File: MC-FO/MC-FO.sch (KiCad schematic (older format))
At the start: 0 parts

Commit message: Add files via upload
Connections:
- wire segments 7 -> 10
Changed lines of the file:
@@
 $Descr A4 11693 8268
 encoding utf-8
-Sheet 1 6
+Sheet 1 12
 Title ""
 Date ""
@@
 Comment4 ""
 $EndDescr
+Text GLabel 7900 1150 0    50   Input ~ 0
+3V3
+Text GLabel 7900 1350 0    50   Input ~ 0
+5V
+$Comp
+L power:GND #PWR?
+U 1 1 6175A5B5
+P 7850 1550
+F 0 "#PWR?" H 7850 1300 50  0001 C CNN
+F 1 "GND" H 7855 1377 50  0000 C CNN
+F 2 "" H 7850 1550 50  0001 C CNN
+F 3 "" H 7850 1550 50  0001 C CNN
+	1    7850 1550
+	1    0    0    -1
+$EndComp
+Wire Wire Line
+	3500 1350 4200 1350
+Wire Wire Line
+	3500 3850 4350 3850
 $Sheet
-S 3150 3100 750  250
+S 2750 6700 750  250
+U 6175C442
+F0 "Sheet6175C441" 50
+F1 "Voltage_Regulation.sch" 50
+F2 "Vdd" I R 3500 6850 50
+$EndSheet
+$Sheet
+S 2750 3100 750  300
+U 61750A2A
+F0 "Emitter3" 50
+F1 "Emitter_Circuits.sch" 50
+F2 "EPWM" I R 3500 3300 50
+$EndSheet
+$Sheet
+S 2750 2600 750  250
+U 617509F7
+F0 "Emmiter2" 50
+F1 "Emitter_Circuits.sch" 50
+F2 "EPWM" I R 3500 2750 50
+$EndSheet
+$Sheet
+S 2750 2050 750  250
 U 61717EAF
 F0 "Emitter1" 50
 F1 "Emitter_Circuits.sch" 50
-F2 "EPWM" I R 3900 3200 50
+F2 "EPWM" I R 3500 2150 50
 $EndSheet
 $Sheet
-S 3150 3600 800  300
-U 617509F7
-F0 "Emmiter2" 50
-F1 "Emitter_Circuits.sch" 50
-F2 "EPWM" I R 3950 3750 50
+S 2750 3700 750  250
+U 6171C819
+F0 "Detector1" 50
+F1 "Detector_Circuits.sch" 50
+F2 "EPWM" I R 3500 3850 50
 $EndSheet
 $Sheet
-S 3150 4200 800  300
-U 61750A2A
-F0 "Emitter3" 50
+S 2750 1200 750  250
+U 6175812E
+F0 "Status LED" 50
+F1 "MC-LED.sch" 50
+F2 "StatusLED" I R 3500 1350 50
+$EndSheet
+Wire Wire Line
+	3500 2150 4100 2150
+$Sheet
+S 2750 6050 750  250
+U 61724A08
+F0 "Detector2" 50
+F1 "Detector_Circuits.sch" 50
+F2 "EPWM" I R 3500 6200 50
+$EndSheet
+Wire Wire Line
+	3500 2750 4200 2750
+Wire Wire Line
+	3500 3300 4200 3300
+Wire Wire Line
+	3500 6850 4200 6850
+Wire Wire Line
+	3500 6200 4350 6200
+$Sheet
+S 2750 700  750  250
+U 61766F1E
+F0 "Power LED" 50
+F1 "MC-Power_LED.sch" 50
+F2 "Vdd" I R 3500 850 50
+$EndSheet
+Wire Wire Line
+	3500 850  4200 850
+Wire Wire Line
+	4200 850  4200 800
+Wire Wire Line
+	4200 800  4250 800
+$Sheet
+S 2750 4350 750  250
+U 6176CA10
+F0 "Emitter4" 50
 F1 "Emitter_Circuits.sch" 50
-F2 "EPWM" I R 3950 4400 50
 $EndSheet
-Text GLabel 5350 2650 0    50   Input ~ 0
-3V3
-Text GLabel 5350 2850 0    50   Input ~ 0
-5V
 $Sheet
-S 3350 2150 600  300
-U 6175812E
-F0 "Sheet6175812D" 50
-F1 "MC-LED.sch" 50
-F2 "StatusLED" I R 3950 2300 50
+S 2750 4900 750  250
+U 6176CA81
+F0 "Emitter5" 50
+F1 "Emitter_Circuits.sch" 50
 $EndSheet
-$Comp
-L power:GND #PWR?
-U 1 1 6175A5B5
-P 5250 3000
-F 0 "#PWR?" H 5250 2750 50  0001 C CNN
-F 1 "GND" H 5255 2827 50  0000 C CNN
-F 2 "" H 5250 3000 50  0001 C CNN
-F 3 "" H 5250 3000 50  0001 C CNN
-	1    5250 3000
-	1    0    0    -1
-$EndComp
-Wire Wire Line
-	3950 2300 4650 2300
-Wire Wire Line
-	4650 2300 4650 3350
-Wire Wire Line
-	4650 3350 5350 3350
-Wire Wire Line
-	5350 3350 5350 3300
-Wire Wire Line
-	3900 3200 4450 3200
-Wire Wire Line
-	4450 3200 4450 3550
-Wire Wire Line
-	4450 3550 5300 3550
 $Sheet
-S 3150 4800 900  250
-U 6175C442
-F0 "Sheet6175C441" 50
-F1 "Voltage_Regulation.sch" 50
-F2 "Vdd" I R 4050 4950 50
+S 2750 5450 750  250
+U 6176CAE4
+F0 "Emitter6" 50
+F1 "Emitter_Circuits.sch" 50
 $EndSheet
 $EndSCHEMATC

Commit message: Add files via upload
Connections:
- wire segments 10 -> 13
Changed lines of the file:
@@
 S 2750 6700 750  250
 U 6175C442
-F0 "Sheet6175C441" 50
+F0 "Voltage Regulation" 50
 F1 "Voltage_Regulation.sch" 50
 F2 "Vdd" I R 3500 6850 50
@@
 F0 "Detector1" 50
 F1 "Detector_Circuits.sch" 50
-F2 "EPWM" I R 3500 3850 50
+F2 "DPWM" I R 3500 3850 50
 $EndSheet
 $Sheet
@@
 F0 "Detector2" 50
 F1 "Detector_Circuits.sch" 50
-F2 "EPWM" I R 3500 6200 50
+F2 "DPWM" I R 3500 6200 50
 $EndSheet
 Wire Wire Line
@@
 F0 "Emitter4" 50
 F1 "Emitter_Circuits.sch" 50
+F2 "EPWM" I R 3500 4500 50
 $EndSheet
 $Sheet
@@
 F0 "Emitter5" 50
 F1 "Emitter_Circuits.sch" 50
+F2 "EPWM" I R 3500 5050 50
 $EndSheet
 $Sheet
@@
 F0 "Emitter6" 50
 F1 "Emitter_Circuits.sch" 50
+F2 "EPWM" I R 3500 5600 50
 $EndSheet
+Wire Wire Line
+	3500 5600 4350 5600
+Wire Wire Line
+	3500 5050 4400 5050
+Wire Wire Line
+	3500 4500 4450 4500
 $EndSCHEMATC

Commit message: Add files via upload
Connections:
- net labels added: 24V, GND1, GND2, GPIO
- wire segments 13 -> 55
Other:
- note added: "is the vreg sheet supposed to supply the 3v3 and 5 v \nvoltages to the detectors and emitters?"
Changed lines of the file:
@@
 $Descr A4 11693 8268
 encoding utf-8
-Sheet 1 12
+Sheet 1 11
 Title ""
 Date ""
@@
 Comment4 ""
 $EndDescr
-Text GLabel 7900 1150 0    50   Input ~ 0
+Text GLabel 10450 5150 0    50   Input ~ 0
 3V3
-Text GLabel 7900 1350 0    50   Input ~ 0
+Text GLabel 10450 5350 0    50   Input ~ 0
 5V
 $Comp
 L power:GND #PWR?
 U 1 1 6175A5B5
-P 7850 1550
-F 0 "#PWR?" H 7850 1300 50  0001 C CNN
-F 1 "GND" H 7855 1377 50  0000 C CNN
-F 2 "" H 7850 1550 50  0001 C CNN
-F 3 "" H 7850 1550 50  0001 C CNN
-	1    7850 1550
+P 10400 5550
+F 0 "#PWR?" H 10400 5300 50  0001 C CNN
+F 1 "GND" H 10405 5377 50  0000 C CNN
+F 2 "" H 10400 5550 50  0001 C CNN
+F 3 "" H 10400 5550 50  0001 C CNN
+	1    10400 5550
 	1    0    0    -1
 $EndComp
 Wire Wire Line
-	3500 1350 4200 1350
-Wire Wire Line
-	3500 3850 4350 3850
-$Sheet
-S 2750 6700 750  250
+	7250 2200 6550 2200
+$Sheet
+S 1500 4500 1000 500
+U 6176CA10
+F0 "Emitter4" 50
+F1 "Emitter_Circuits.sch" 50
+F2 "EPWM" I R 2500 4650 50
+F3 "5V" I R 2500 4800 50
+F4 "GND2" I R 2500 4900 50
+$EndSheet
+$Sheet
+S 1500 5500 1000 500
+U 6176CA81
+F0 "Emitter5" 50
+F1 "Emitter_Circuits.sch" 50
+F2 "EPWM" I R 2500 5600 50
+F3 "5V" I R 2500 5750 50
+F4 "GND2" I R 2500 5900 50
+$EndSheet
+$Sheet
+S 1500 6500 1000 500
+U 6176CAE4
+F0 "Emitter6" 50
+F1 "Emitter_Circuits.sch" 50
+F2 "EPWM" I R 2500 6600 50
+F3 "5V" I R 2500 6750 50
+F4 "GND2" I R 2500 6900 50
+$EndSheet
+$Sheet
+S 1500 1500 1000 500
+U 61717EAF
+F0 "Emitter1" 50
+F1 "Emitter_Circuits.sch" 50
+F2 "EPWM" I R 2500 1600 50
+F3 "5V" I R 2500 1750 50
+F4 "GND2" I R 2500 1900 50
+$EndSheet
+$Sheet
+S 1500 2500 1000 500
+U 617509F7
+F0 "Emmiter2" 50
+F1 "Emitter_Circuits.sch" 50
+F2 "EPWM" I R 2500 2600 50
+F3 "5V" I R 2500 2750 50
+F4 "GND2" I R 2500 2900 50
+$EndSheet
+$Sheet
+S 1500 3500 1000 500
+U 61750A2A
+F0 "Emitter3" 50
+F1 "Emitter_Circuits.sch" 50
+F2 "EPWM" I R 2500 3700 50
+F3 "5V" I R 2500 3850 50
+F4 "GND2" I R 2500 3950 50
+$EndSheet
+Text HLabel 9300 800  2    79   Input ~ 0
+24V
+Wire Wire Line
+	2500 2600 3200 2600
+Wire Wire Line
+	2500 3700 3200 3700
+Wire Wire Line
+	2500 4650 3250 4650
+Wire Wire Line
+	2500 5600 3400 5600
+Wire Wire Line
+	2500 1600 3100 1600
+Wire Wire Line
+	3500 1750 2500 1750
+Wire Wire Line
+	3500 6750 2500 6750
+Wire Wire Line
+	2500 5750 3500 5750
+Connection ~ 3500 5750
+Wire Wire Line
+	2500 4800 3500 4800
+Connection ~ 3500 4800
+Wire Wire Line
+	2500 3850 3500 3850
+Connection ~ 3500 3850
+Wire Wire Line
+	3500 3850 3500 4750
+Wire Wire Line
+	2500 2750 3500 2750
+Connection ~ 3500 2750
+Wire Wire Line
+	3500 4800 3500 4750
+Connection ~ 3500 4750
+Wire Wire Line
+	3500 5750 3500 6750
+Wire Wire Line
+	4950 5750 3500 5750
+Wire Wire Line
+	4950 4750 3500 4750
+Wire Wire Line
+	4950 5600 4100 5600
+$Sheet
+S 4950 5500 1000 500
+U 61724A08
+F0 "Detector2" 50
+F1 "Detector_Circuits.sch" 50
+F2 "DPWM" I L 4950 5600 50
+F3 "5V" I L 4950 5750 50
+F4 "GND2" I L 4950 5900 50
+$EndSheet
+$Sheet
+S 4950 4500 1000 500
+U 6171C819
+F0 "Detector1" 50
+F1 "Detector_Circuits.sch" 50
+F2 "DPWM" I L 4950 4600 50
+F3 "5V" I L 4950 4750 50
+F4 "GND2" I L 4950 4900 50
+$EndSheet
+Wire Wire Line
+	4950 4600 4100 4600
+$Sheet
+S 7250 1150 1000 500
 U 6175C442
 F0 "Voltage Regulation" 50
 F1 "Voltage_Regulation.sch" 50
-F2 "Vdd" I R 3500 6850 50
-$EndSheet
-$Sheet
-S 2750 3100 750  300
-U 61750A2A
-F0 "Emitter3" 50
-F1 "Emitter_Circuits.sch" 50
-F2 "EPWM" I R 3500 3300 50
-$EndSheet
-$Sheet
-S 2750 2600 750  250
-U 617509F7
-F0 "Emmiter2" 50
-F1 "Emitter_Circuits.sch" 50
-F2 "EPWM" I R 3500 2750 50
-$EndSheet
-$Sheet
-S 2750 2050 750  250
-U 61717EAF
-F0 "Emitter1" 50
-F1 "Emitter_Circuits.sch" 50
-F2 "EPWM" I R 3500 2150 50
-$EndSheet
-$Sheet
-S 2750 3700 750  250
-U 6171C819
-F0 "Detector1" 50
-F1 "Detector_Circuits.sch" 50
-F2 "DPWM" I R 3500 3850 50
-$EndSheet
-$Sheet
-S 2750 1200 750  250
+F2 "Vdd" I R 8250 1300 50
+F3 "3V3" I L 7250 1550 50
+F4 "5V" I L 7250 1250 50
+F5 "GND1" I L 7250 1400 50
+$EndSheet
+Text Notes 6250 1000 0    50   ~ 0
+is the vreg sheet supposed to supply the 3v3 and 5 v \nvoltages to the detectors and emitters?
+Wire Wire Line
+	3500 2750 3500 3850
+$Sheet
+S 7250 2100 1000 500
 U 6175812E
 F0 "Status LED" 50
 F1 "MC-LED.sch" 50
-F2 "StatusLED" I R 3500 1350 50
-$EndSheet
-Wire Wire Line
-	3500 2150 4100 2150
-$Sheet
-S 2750 6050 750  250
-U 61724A08
-F0 "Detector2" 50
-F1 "Detector_Circuits.sch" 50
-F2 "DPWM" I R 3500 6200 50
-$EndSheet
-Wire Wire Line
-	3500 2750 4200 2750
-Wire Wire Line
-	3500 3300 4200 3300
-Wire Wire Line
-	3500 6850 4200 6850
-Wire Wire Line
-	3500 6200 4350 6200
-$Sheet
-S 2750 700  750  250
-U 61766F1E
-F0 "Power LED" 50
-F1 "MC-Power_LED.sch" 50
-F2 "Vdd" I R 3500 850 50
-$EndSheet
-Wire Wire Line
-	3500 850  4200 850
-Wire Wire Line
-	4200 850  4200 800
-Wire Wire Line
-	4200 800  4250 800
-$Sheet
-S 2750 4350 750  250
-U 6176CA10
-F0 "Emitter4" 50
-F1 "Emitter_Circuits.sch" 50
-F2 "EPWM" I R 3500 4500 50
-$EndSheet
-$Sheet
-S 2750 4900 750  250
-U 6176CA81
-F0 "Emitter5" 50
-F1 "Emitter_Circuits.sch" 50
-F2 "EPWM" I R 3500 5050 50
-$EndSheet
-$Sheet
-S 2750 5450 750  250
-U 6176CAE4
-F0 "Emitter6" 50
-F1 "Emitter_Circuits.sch" 50
-F2 "EPWM" I R 3500 5600 50
-$EndSheet
-Wire Wire Line
-	3500 5600 4350 5600
-Wire Wire Line
-	3500 5050 4400 5050
-Wire Wire Line
-	3500 4500 4450 4500
+F2 "StatusLED" I L 7250 2200 50
+F3 "3V3" I L 7250 2350 50
+F4 "GND1" I L 7250 2500 50
+$EndSheet
+Wire Wire Line
+	9300 800  8750 800
+Wire Wire Line
+	8750 800  8750 1300
+Wire Wire Line
+	8250 1300 8750 1300
+Connection ~ 3500 1750
+Wire Wire Line
+	3500 1750 3500 2750
+Wire Wire Line
+	7250 1250 3500 1250
+Wire Wire Line
+	3500 1250 3500 1750
+Wire Wire Line
+	7250 1550 5550 1550
+Wire Wire Line
+	5550 1550 5550 2350
+Wire Wire Line
+	5550 2350 7250 2350
+Wire Wire Line
+	2500 1900 2850 1900
+Wire Wire Line
+	2850 1900 2850 2900
+Wire Wire Line
+	2500 6900 2850 6900
+Wire Wire Line
+	2850 6900 2850 6950
+Connection ~ 2850 6900
+Wire Wire Line
+	2500 5900 2850 5900
+Connection ~ 2850 5900
+Wire Wire Line
+	2850 5900 2850 6900
+Wire Wire Line
+	2500 3950 2850 3950
+Connection ~ 2850 3950
+Wire Wire Line
+	2850 3950 2850 4900
+Wire Wire Line
+	2500 4900 2850 4900
+Connection ~ 2850 4900
+Wire Wire Line
+	2850 4900 2850 5900
+Wire Wire Line
+	2500 2900 2850 2900
+Connection ~ 2850 2900
+Wire Wire Line
+	2850 2900 2850 3950
+Wire Wire Line
+	3200 6600 3200 6550
+Wire Wire Line
+	2500 6600 3200 6600
+Wire Wire Line
+	3500 4800 3500 5750
+Wire Wire Line
+	4950 4900 4300 4900
+Wire Wire Line
+	4300 4900 4300 5900
+Wire Wire Line
+	4950 5900 4300 5900
+Connection ~ 4300 5900
+Wire Wire Line
+	4300 5900 4300 6950
+$Comp
+L power:GND1 #PWR?
+U 1 1 617C7B3D
+P 6850 2950
+F 0 "#PWR?" H 6850 2700 50  0001 C CNN
+F 1 "GND1" H 6855 2777 50  0000 C CNN
+F 2 "" H 6850 2950 50  0001 C CNN
+F 3 "" H 6850 2950 50  0001 C CNN
+	1    6850 2950
+	1    0    0    -1
+$EndComp
+Wire Wire Line
+	7250 1400 6850 1400
+Wire Wire Line
+	6850 1400 6850 2500
+Wire Wire Line
+	7250 2500 6850 2500
+Connection ~ 6850 2500
+$Comp
+L power:GND2 #PWR?
+U 1 1 617BB8F9
+P 3750 7350
+F 0 "#PWR?" H 3750 7100 50  0001 C CNN
+F 1 "GND2" H 3755 7177 50  0000 C CNN
+F 2 "" H 3750 7350 50  0001 C CNN
+F 3 "" H 3750 7350 50  0001 C CNN
+	1    3750 7350
+	1    0    0    -1
+$EndComp
+Wire Wire Line
+	3750 6950 3750 7350
+Wire Wire Line
+	2850 6950 3750 6950
+Wire Wire Line
+	4300 6950 3750 6950
+Connection ~ 3750 6950
+Text HLabel 6550 2200 0    50   Input ~ 0
+GPIO
+Wire Wire Line
+	6850 2500 6850 2950
 $EndSCHEMATC

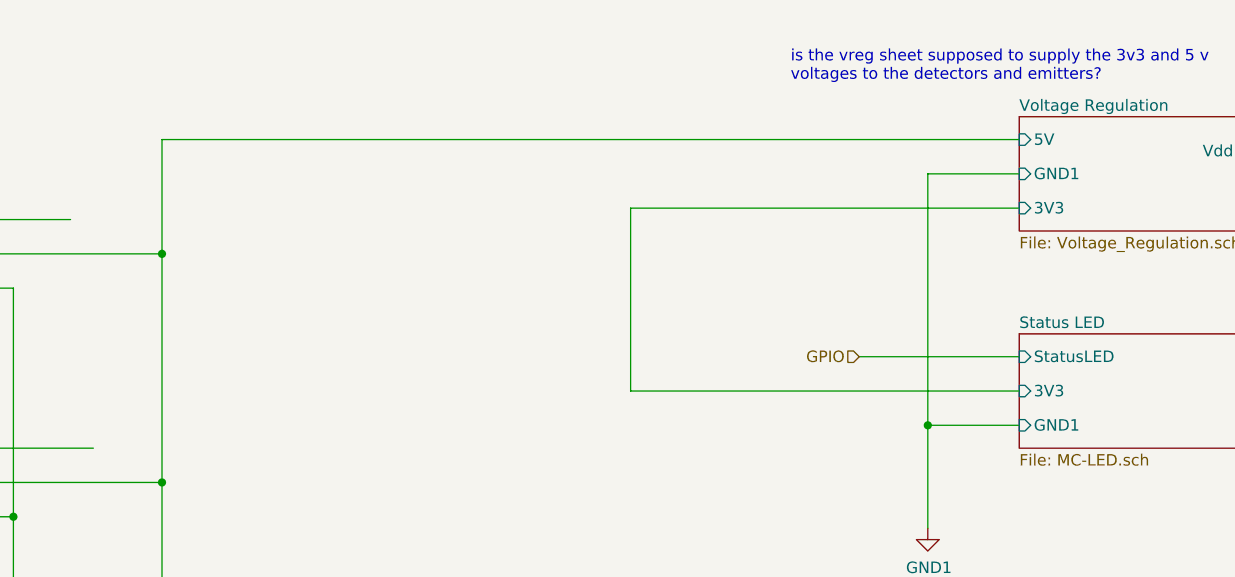
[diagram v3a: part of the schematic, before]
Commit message: Updated LED Ckts, Added new IC model
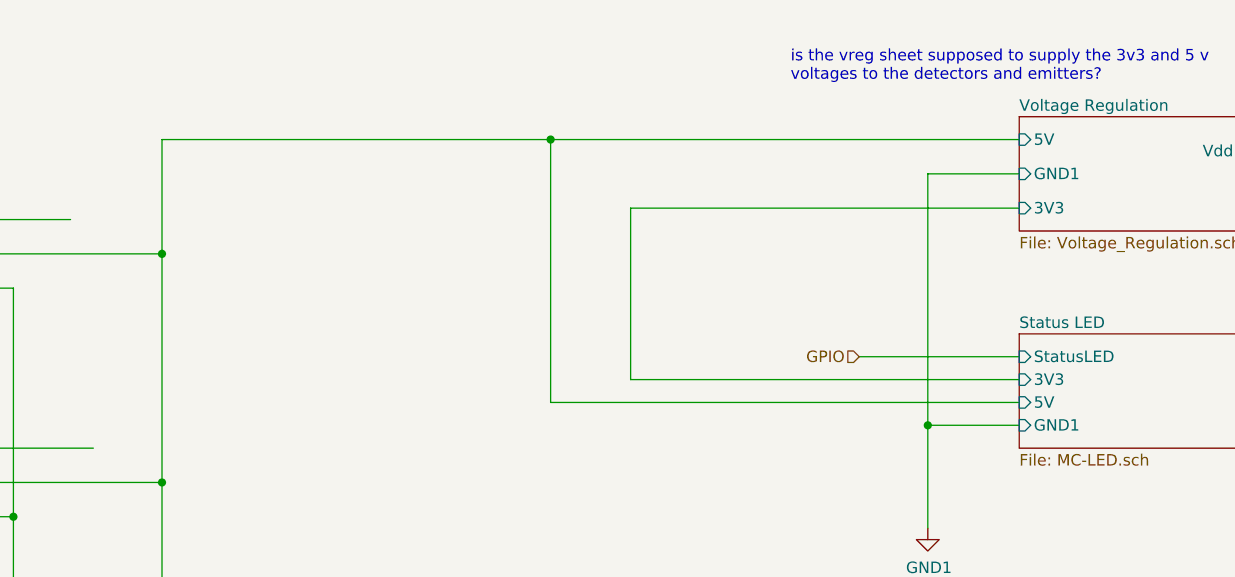
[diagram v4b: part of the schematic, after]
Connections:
- wire segments 55 -> 58
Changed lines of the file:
@@
 F1 "MC-LED.sch" 50
 F2 "StatusLED" I L 7250 2200 50
-F3 "3V3" I L 7250 2350 50
+F3 "3V3" I L 7250 2300 50
 F4 "GND1" I L 7250 2500 50
+F5 "5V" I L 7250 2400 50
 $EndSheet
 Wire Wire Line
@@
 	3500 1750 3500 2750
 Wire Wire Line
-	7250 1250 3500 1250
+	7250 1250 5200 1250
 Wire Wire Line
 	3500 1250 3500 1750
@@
 	7250 1550 5550 1550
 Wire Wire Line
-	5550 1550 5550 2350
+	5550 1550 5550 2300
 Wire Wire Line
-	5550 2350 7250 2350
+	5550 2300 7250 2300
 Wire Wire Line
 	2500 1900 2850 1900
@@
 Wire Wire Line
 	6850 2500 6850 2950
+Wire Wire Line
+	5200 1250 5200 2400
+Wire Wire Line
+	5200 2400 7250 2400
+Connection ~ 5200 1250
+Wire Wire Line
+	5200 1250 3500 1250
 $EndSCHEMATC

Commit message: Add files via upload
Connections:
- net labels removed: 3V3, 5V, GND
- wire segments 58 -> 59
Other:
- note removed: "is the vreg sheet supposed to supply the 3v3 and 5 v \nvoltages to the detectors and emitters?"
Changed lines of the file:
@@
 Comment4 ""
 $EndDescr
-Text GLabel 10450 5150 0    50   Input ~ 0
-3V3
-Text GLabel 10450 5350 0    50   Input ~ 0
-5V
-$Comp
-L power:GND #PWR?
-U 1 1 6175A5B5
-P 10400 5550
-F 0 "#PWR?" H 10400 5300 50  0001 C CNN
-F 1 "GND" H 10405 5377 50  0000 C CNN
-F 2 "" H 10400 5550 50  0001 C CNN
-F 3 "" H 10400 5550 50  0001 C CNN
-	1    10400 5550
-	1    0    0    -1
-$EndComp
 Wire Wire Line
 	7250 2200 6550 2200
@@
 F5 "GND1" I L 7250 1400 50
 $EndSheet
-Text Notes 6250 1000 0    50   ~ 0
-is the vreg sheet supposed to supply the 3v3 and 5 v \nvoltages to the detectors and emitters?
 Wire Wire Line
 	3500 2750 3500 3850
@@
 Wire Wire Line
 	4300 5900 4300 6950
-$Comp
-L power:GND1 #PWR?
-U 1 1 617C7B3D
-P 6850 2950
-F 0 "#PWR?" H 6850 2700 50  0001 C CNN
-F 1 "GND1" H 6855 2777 50  0000 C CNN
-F 2 "" H 6850 2950 50  0001 C CNN
-F 3 "" H 6850 2950 50  0001 C CNN
-	1    6850 2950
-	1    0    0    -1
-$EndComp
 Wire Wire Line
 	7250 1400 6850 1400
@@
 	7250 2500 6850 2500
 Connection ~ 6850 2500
-$Comp
-L power:GND2 #PWR?
-U 1 1 617BB8F9
-P 3750 7350
-F 0 "#PWR?" H 3750 7100 50  0001 C CNN
-F 1 "GND2" H 3755 7177 50  0000 C CNN
-F 2 "" H 3750 7350 50  0001 C CNN
-F 3 "" H 3750 7350 50  0001 C CNN
-	1    3750 7350
-	1    0    0    -1
-$EndComp
 Wire Wire Line
 	3750 6950 3750 7350
@@
 Wire Wire Line
 	5200 1250 3500 1250
+Text HLabel 6700 2950 0    50   Input ~ 0
+GND1
+Wire Wire Line
+	6850 2950 6700 2950
+Text HLabel 3750 7350 0    50   Input ~ 0
+GND2
 $EndSCHEMATC
